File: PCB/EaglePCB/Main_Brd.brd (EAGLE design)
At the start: 99.1 x 85.1 mm, 67 parts, among them U1 ATWINC1500-MR210PB1952-T, U3 MSP430FR2355TDBTRDBT0038A_M, U6 ARJM11C7-114-BA-EW2

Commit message: Final Revision V1.1 for Print
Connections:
- new net 3.3: U3.38
- new net 3.5: U3.34
- new net 3.6: U3.33
- new net 3.7: U3.32
- new net 5.0: U3.37
- new net 5.1: U3.36
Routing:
- net 3.7: track 0.00 -> 7.04 mm, vias 0 -> 1
- net 3.6: track 0.00 -> 6.01 mm, vias 0 -> 1
- net 3.5: track 0.00 -> 4.99 mm, vias 0 -> 1
- net 5.1: track 0.00 -> 3.89 mm, vias 0 -> 1
- net 5.0: track 0.00 -> 3.59 mm, vias 0 -> 1
- net 3.3: track 0.00 -> 2.29 mm, vias 0 -> 1
- net OSC2_ETH: track 10.9 -> 10.4 mm
- net GND: vias 197 -> 195
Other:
- board text added: "25MHz"
- board text added: "ATWINC1500"
- board text added: "LoRa Receive"
- board text added: "LoRa Send"
- board text added: "MSP430"
- board text added: "Magic WiFi 1.0"
- board text added: "TI-JTAG"

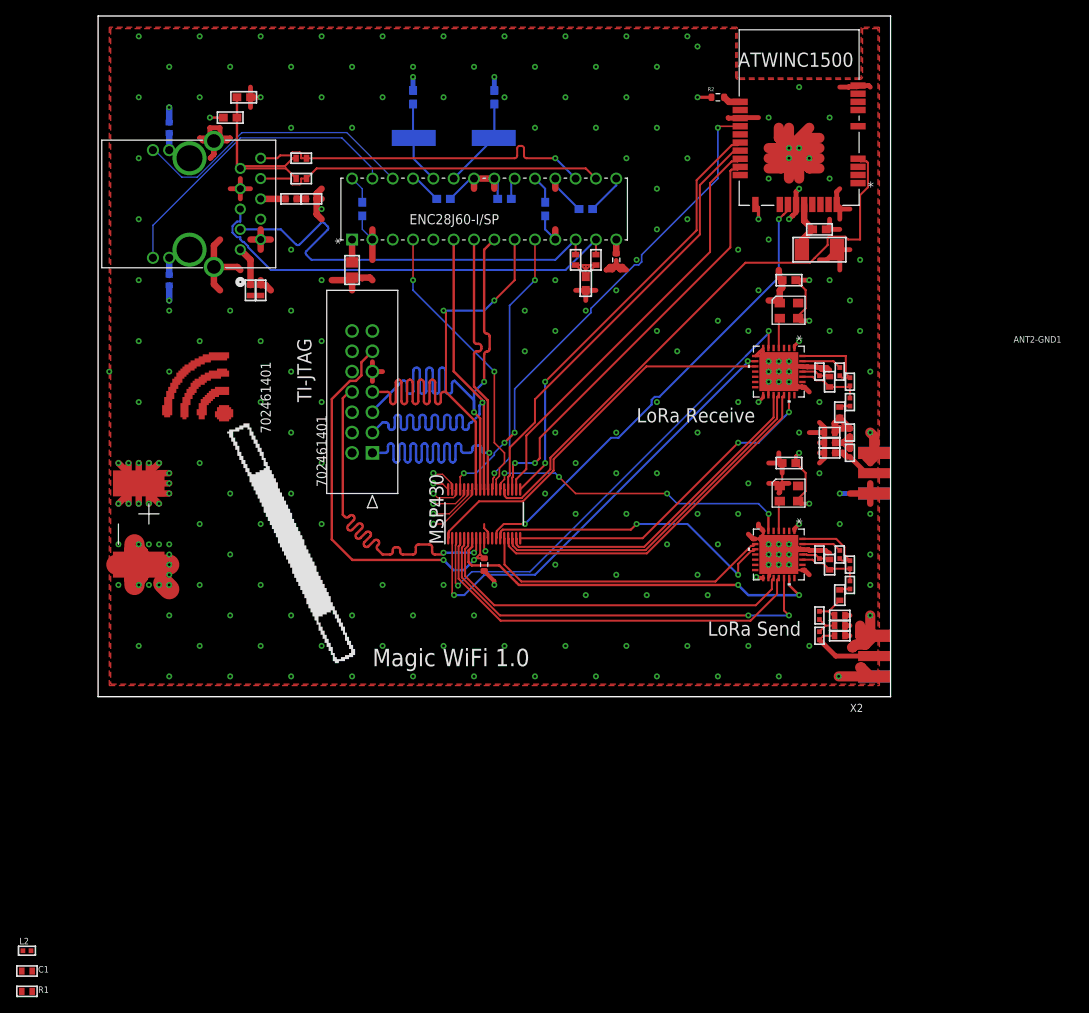
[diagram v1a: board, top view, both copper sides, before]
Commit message: fixed top ground plane issue
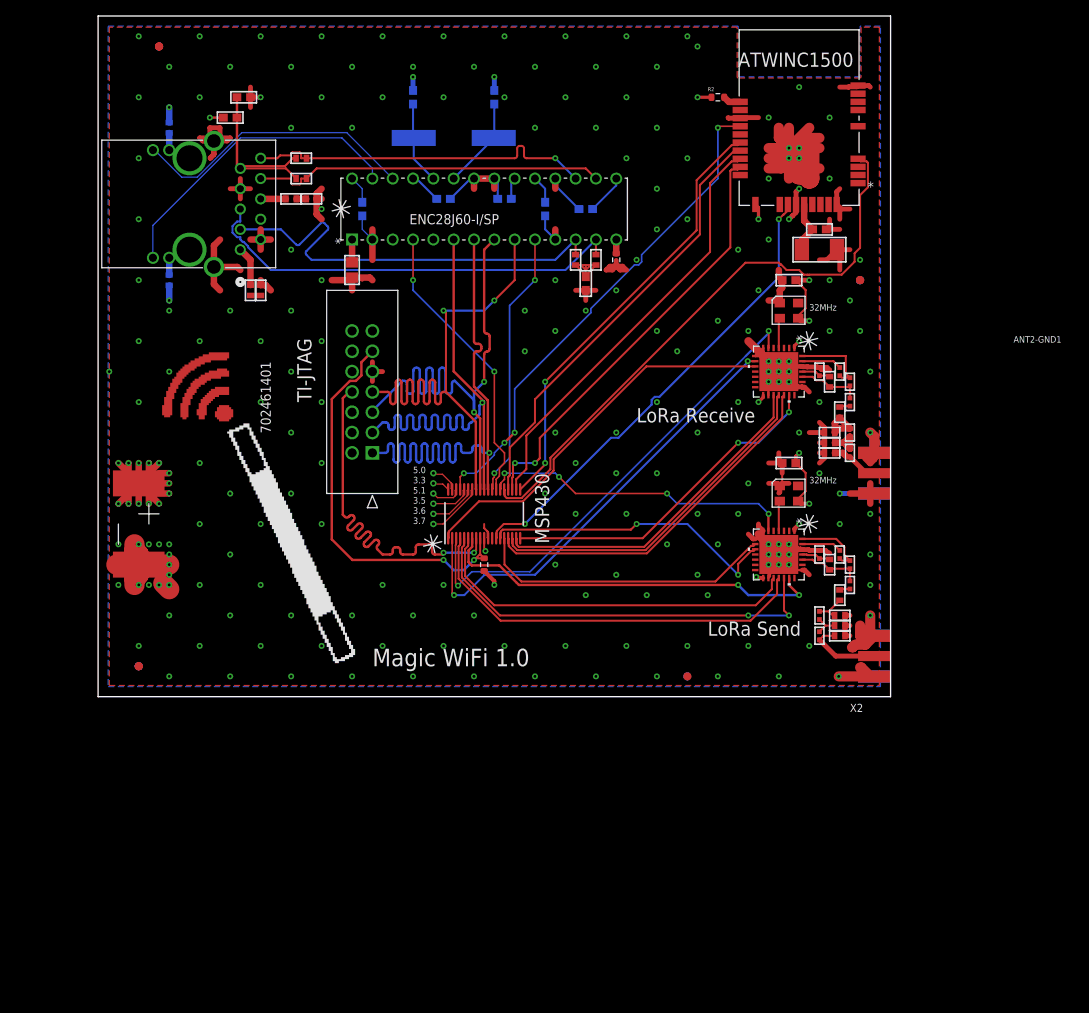
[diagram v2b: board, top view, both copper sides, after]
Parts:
- removed C1, R1: (no value), microbuilder:0402
- removed L2: (no value), microbuilder:_0402
- added FD1, FD2, FD3, FD4, FD5, FD6, FD7: FID_40MIL, Fiducial:FID_040
- added U$10, U$11, U$12, U$9: PIN_MARKER, 473:PIN_MARKER
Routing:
- net GND: track 329.7 -> 335.7 mm
- net !ATC_RST: track 71.9 -> 73.5 mm
- added copper zone on layer 16, net 3V3
- removed copper zone on layer 1, net 3V3
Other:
- board text added: "3.3"
- board text added: "3.5"
- board text added: "3.6"
- board text added: "3.7"
- board text added: "32MHz"
- board text added: "5.0"
- board text added: "5.1"

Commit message: EaglePCB Changes: - Converted 4 layer to 2 layer for cost savings - Removed Fiducials for simplicity - Switched MOSI/MISO on LoRa1 for correctness
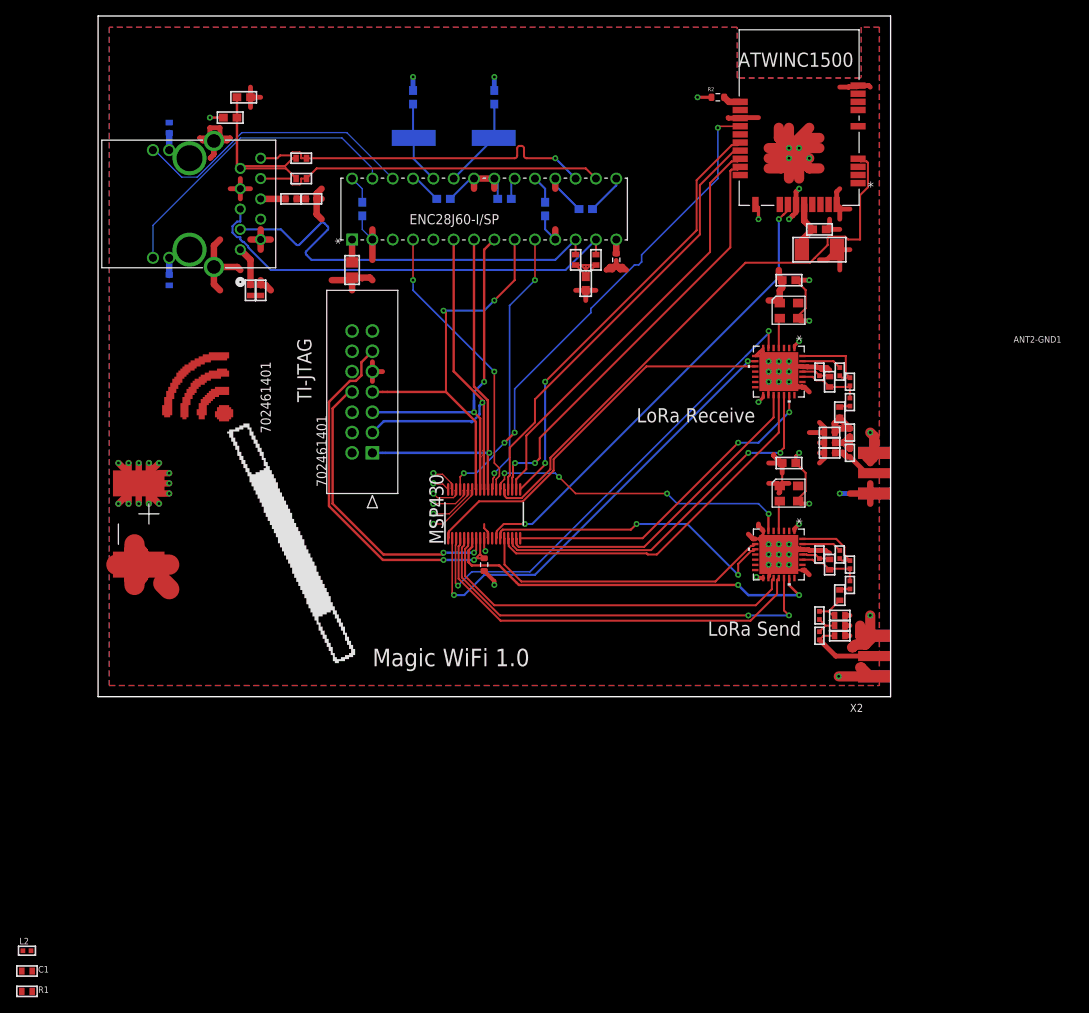
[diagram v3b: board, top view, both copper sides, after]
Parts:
- removed FD1, FD2, FD3, FD4, FD5, FD6, FD7: FID_40MIL, Fiducial:FID_040
- removed U$10, U$11, U$12, U$9: PIN_MARKER, 473:PIN_MARKER
- added C1, R1: (no value), microbuilder:0402
- added L2: (no value), microbuilder:_0402
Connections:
- net LORA1_MISO: now also LORA1.18; no longer LORA1.19
- net LORA1_MOSI: now also LORA1.19; no longer LORA1.18
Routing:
- net ETH_MOSI: track 74.0 -> 46.8 mm
- net !ETH_CHIPSEL: track 72.1 -> 48.8 mm
- net ETH_CLK: track 69.7 -> 46.8 mm
- net 3V3: track 110.8 -> 89.0 mm, vias 29 -> 27
- net ETH_MISO: track 67.6 -> 49.2 mm
- net MSP_TEST: track 47.9 -> 37.6 mm
- net GND: track 335.7 -> 328.6 mm, vias 195 -> 28
- net LORA1_MOSI: track 44.0 -> 47.1 mm, vias 0 -> 2
- net !MSP_RST: track 51.1 -> 48.1 mm
- net !ATC_RST: track 73.5 -> 71.9 mm
- net LORA1_MISO: track 45.5 -> 46.2 mm
- net !ETH_IRQ: track 36.4 -> 35.9 mm
- removed copper zone on layer 15, net 3V3
- removed copper zone on layer 2, net GND
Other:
- board text removed: "3.3"
- board text removed: "3.5"
- board text removed: "3.6"
- board text removed: "3.7"
- board text removed: "32MHz"
- board text removed: "5.0"
- board text removed: "5.1"

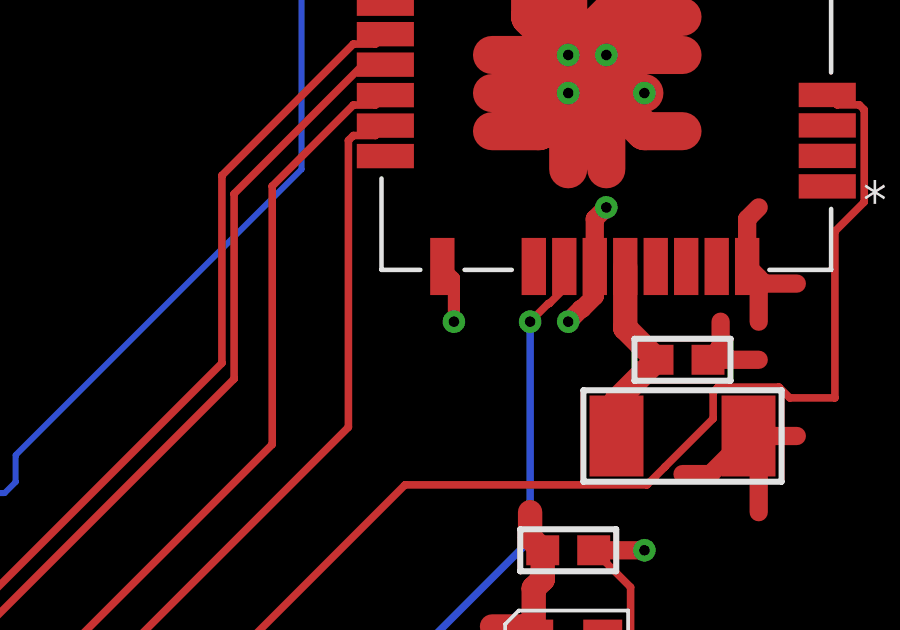
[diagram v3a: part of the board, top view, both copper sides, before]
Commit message: Connected VBatt to 3v3 ATWinC
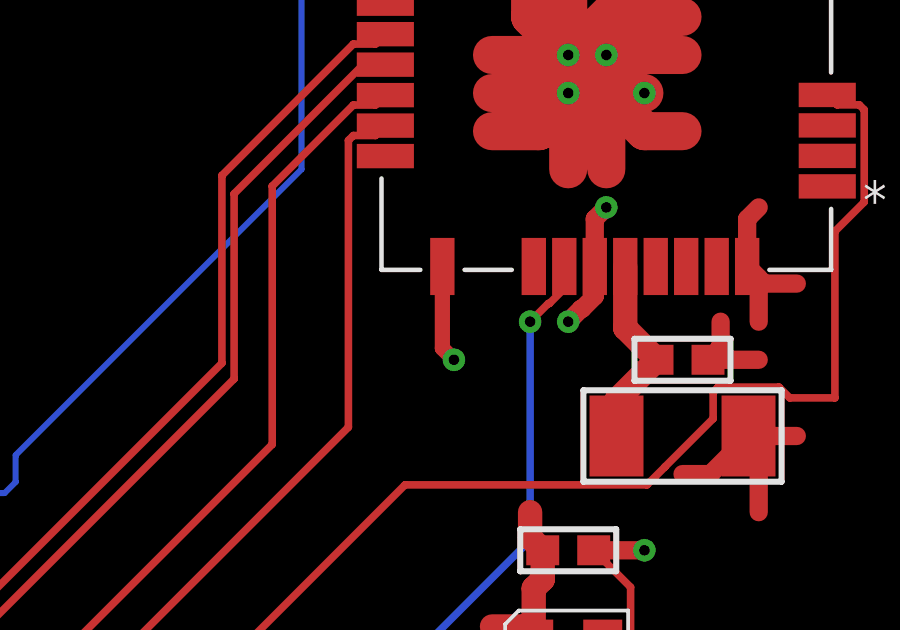
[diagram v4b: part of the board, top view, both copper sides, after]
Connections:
- removed net VBAT: U1.20
- net 3V3: now also U1.20
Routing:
- net 3V3: track 89.0 -> 92.3 mm, vias 27 -> 28
- net VBAT: track 2.00 -> 0.00 mm, vias 1 -> 0
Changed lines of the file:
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@@
 </elements>
 <signals>
-<signal name="VBAT">
-<contactref element="U1" pad="20"/>
-<wire x1="82.165" y1="61.53" x2="82.55" y2="61.145" width="0.4064" layer="1"/>
-<wire x1="82.55" y1="61.145" x2="82.55" y2="59.69" width="0.4064" layer="1"/>
-<via x="82.55" y="59.69" extent="1-16" drill="0.35"/>
-</signal>
 <signal name="GND">
 <contactref element="RFI-GND" pad="2"/>
@@
 <vertex x="95.357665625" y="77.398059375"/>
 </polygon>
+<contactref element="U1" pad="20"/>
+<wire x1="82.165" y1="61.53" x2="82.165" y2="58.805" width="0.508" layer="1"/>
+<wire x1="82.165" y1="58.805" x2="82.55" y2="58.42" width="0.508" layer="1"/>
+<via x="82.55" y="58.42" extent="1-16" drill="0.35"/>
 <wire x1="48.4176" y1="18.2056" x2="48.26" y2="18.3632" width="0" layer="19" extent="1-1"/>
 </signal>
